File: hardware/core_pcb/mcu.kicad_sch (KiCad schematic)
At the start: 33 parts, among them J5 SWD, J6 SERVICE UART, SW1 RESET, U3 STM32H573VIT6, Y1 25MHz, Y2 32.768kHz

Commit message: Core PCB: add the 8 MB QSPI PSRAM (APS6404L) on OCTOSPI1
Gary approved the PSRAM (29 Oct) for working RAM headroom. U10 on PB2 CLK,
PB10 NCS, PB1/PB0/PC2/PA6 IO0-3 (pins agreed with the RAM thread, all
previously free), 33R series on CLK, 10k pull-up on NCS, 100n + 1u.
Project symbol APS6404L derived from KiCad's ESP-PSRAM32 (same pinout).

Co-Authored-By: Claude Opus 5.5 <noreply@anthropic.com>
Claude-Session: https://claude.ai/code/session_014onnq3eRiDkqdAB6fKiRDW
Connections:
- net PSRAM_IO2: now reaches U3.17 (PC2)
- net PSRAM_IO3: now reaches U3.31 (PA6)
- net PSRAM_IO1: now reaches U3.35 (PB0)
- net PSRAM_IO0: now reaches U3.36 (PB1)
- net PSRAM_CLK_MCU: now reaches U3.37 (PB2)
- net PSRAM_NCS: now reaches U3.47 (PB10)
- no-connect marks 43 -> 37
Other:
- moved on the sheet: C20, C23, C24, C29, C30, C33, D11, FB1, J6, JP1, R20, R21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

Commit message: Core PCB: board role jumper J7 on PE5/PE6 (CORE or I/O node)
3-pin header, GND centre, 10k pull-ups and 100n per pin. 1-2 = CORE
(PE5=0, PE6=1), 2-3 = I/O node (PE5=1, PE6=0), anything else invalid.
CORE_PCB.md section 12 and the pin map updated.

Co-Authored-By: Claude Opus 5.5 <noreply@anthropic.com>
Claude-Session: https://claude.ai/code/session_014onnq3eRiDkqdAB6fKiRDW
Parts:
- added C36, C37: 100n, Capacitor_SMD:C_0603_1608Metric, symbol Device:C
- added J7: ROLE, Connector_PinHeader_2.54mm:PinHeader_1x03_P2.54mm_Vertical, symbol Connector_Generic:Conn_01x03
- added R27, R28: 10k, Resistor_SMD:R_0603_1608Metric, symbol Device:R
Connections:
- net +3V3: now also R27.1, R28.1
- net GND: now also C36.2, C37.2, J7.2 (Pin_2)
- net ROLE_A: now reaches U3.4 (PE5)
- net ROLE_A: now also C36.1, J7.1 (Pin_1), R27.2
- net ROLE_B: now reaches U3.5 (PE6)
- net ROLE_B: now also C37.1, J7.3 (Pin_3), R28.2
- no-connect marks 37 -> 35
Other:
- note added: "FB1: VDDA / VREF+ filter C29: VCAP, CHECK value and count against the H5 datasheet Y1: HSE, CL 10 pF class. CHECK against the DK C31: CHECK for the crystal's CL Y2: CL 6 pF, ESR per AN2867 C33: AN2867, CHECK for the crystal JP1: fit a jumper for the ST bootloader"
- note added: "J6: FTDI TTL-232R-3V3 order: 1 GND, 2 CTS, 3 VCC (not connected), 4 cable TXD, 5 cable RXD, 6 RTS R23: hardware revision 0: both pulled down R25: NOT FITTED. R26: NOT FITTED. J7: shunt with pull tab; silkscreen 1-2 CORE / 2-3 I/O NODE / none = OFF; reachable only with the housing open C36: ESD, at J7"
- note added: "Notes U3: STM32H563VIT6 is pin-compatible C20: one per VDD pin, VDDUSB included C21: one per VDD pin, VDDUSB included C22: one per VDD pin, VDDUSB included C23: one per VDD pin, VDDUSB included C24: one per VDD pin, VDDUSB included C25: one per VDD pin, VDDUSB included"
- note removed: "C25: one per VDD pin, VDDUSB included FB1: VDDA / VREF+ filter C29: VCAP, CHECK value and count against the H5 datasheet Y1: HSE, CL 10 pF class. CHECK against the DK C31: CHECK for the crystal's CL Y2: CL 6 pF, ESR per AN2867"
- note removed: "C33: AN2867, CHECK for the crystal JP1: fit a jumper for the ST bootloader J6: FTDI TTL-232R-3V3 order: 1 GND, 2 CTS, 3 VCC (not connected), 4 cable TXD, 5 cable RXD, 6 RTS R23: hardware revision 0: both pulled down R25: NOT FITTED. R26: NOT FITTED."
- note removed: "Notes U3: STM32H563VIT6 is pin-compatible C20: one per VDD pin, VDDUSB included C21: one per VDD pin, VDDUSB included C22: one per VDD pin, VDDUSB included C23: one per VDD pin, VDDUSB included C24: one per VDD pin, VDDUSB included"

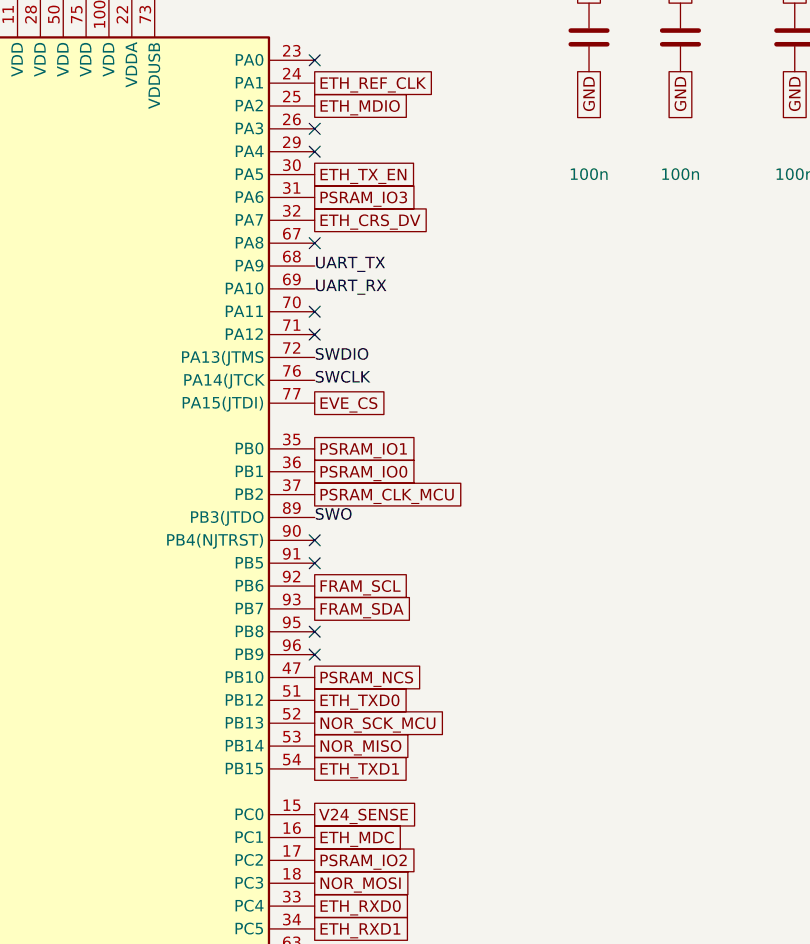
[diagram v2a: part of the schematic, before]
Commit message: Core PCB: RMII series terminations and the any-switch / 100 m design rules
33R source series resistors on TX_EN/TXD0/TXD1 (at the MCU) and
CRS_DV/RXD0/RXD1 (at the PHY), as on ST's DK. CORE_PCB.md 7 records what
the 100 m / any-switch requirement (Gary, 30 Oct) rests on: PHY crystal and
REFCLKO, MODE 111 auto-negotiation (never forced), PHY reset under firmware
control, reference line termination and differential-pair routing.

Co-Authored-By: Claude Opus 5.5 <noreply@anthropic.com>
Claude-Session: https://claude.ai/code/session_014onnq3eRiDkqdAB6fKiRDW
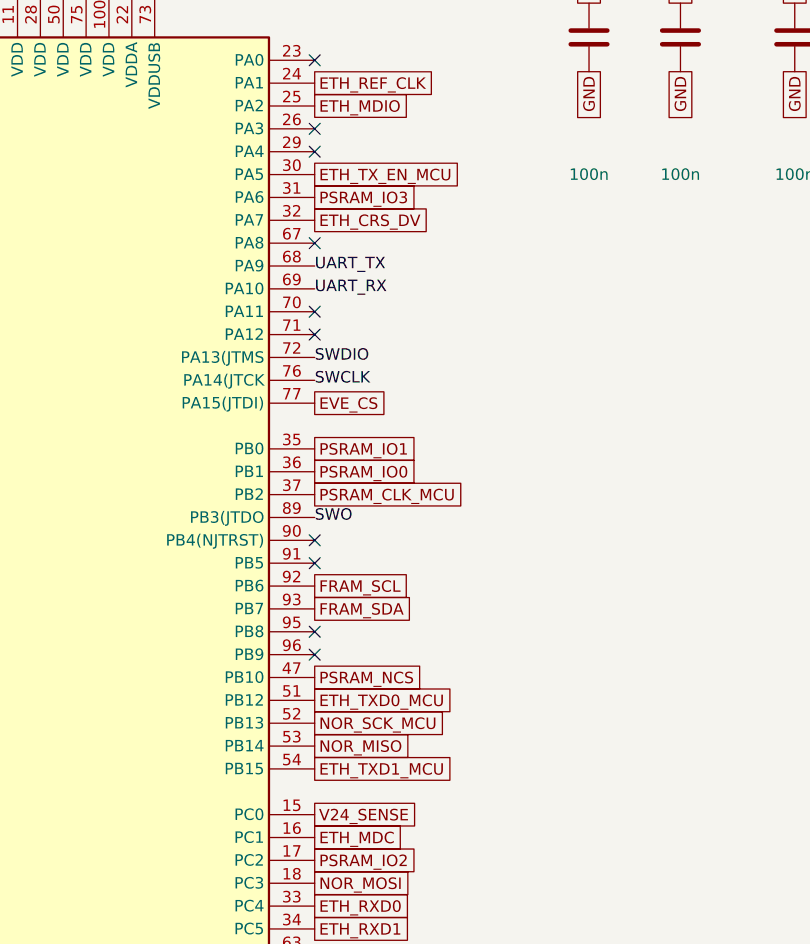
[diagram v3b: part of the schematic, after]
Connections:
- net ETH_TXD0 renamed ETH_TXD0_MCU
- net ETH_TXD1 renamed ETH_TXD1_MCU
- net ETH_TX_EN renamed ETH_TX_EN_MCU

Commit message: CORE PCB rev 0.2: I/O node section on the same board
Three new sheets: field digital I/O with the hardware output gate (ISO2H823V2.5,
ISO808A-1, ISO1I813T), field power / pump / relay coils / USB-C, and the isolated
analog (AD4112) and temperature (ADS124S08) islands. Project symbols for the six
I/O chips missing from KiCad. SPI4 nets renamed: the bus is shared with the I/O chips.
423 parts, netlist check passes. CORE_PCB.md: pin map, connectors, BOM, section 14.

Co-Authored-By: Claude Opus 5.5 <noreply@anthropic.com>
Claude-Session: https://claude.ai/code/session_014onnq3eRiDkqdAB6fKiRDW
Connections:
- net CS_A: now reaches U3.1 (PE2)
- net CS_B: now reaches U3.2 (PE3)
- net PUMP_TACH: now reaches U3.23 (PA0)
- net CS_IN: now reaches U3.3 (PE4)
- net CS_T: now reaches U3.46 (PE15)
- net GATE_FB: now reaches U3.55 (PD8)
- net B_FAULT: now reaches U3.61 (PD14)
- net B_PGOOD: now reaches U3.62 (PD15)
- net PUMP_DIR: now reaches U3.63 (PC6)
- net PUMP_EN: now reaches U3.64 (PC7)
- net USB_VBUS_SNS: now reaches U3.65 (PC8)
- net PUMP_PWM: now reaches U3.67 (PA8)
- net IN_ERR: now reaches U3.7 (PC13)
- net USB_DM: now reaches U3.70 (PA11)
- net USB_DP: now reaches U3.71 (PA12)
- net A_ERR: now reaches U3.82 (PD1)
- net REL1_N: now reaches U3.90 (PB4(NJTRST))
- net REL2_N: now reaches U3.91 (PB5)
- net GATE_EN: now reaches U3.95 (PB8)
- net WDI: now reaches U3.96 (PB9)
- net CS_AI: now reaches U3.97 (PE0)
- net W5500_MISO renamed SPI4_MISO
- net W5500_MOSI_MCU renamed SPI4_MOSI_MCU
- net W5500_SCK_MCU renamed SPI4_SCK_MCU
- no-connect marks 35 -> 14
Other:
- moved on the sheet: C20, C23, C24, C29, C30, C33, C36, C37, D11, FB1, J6, J7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
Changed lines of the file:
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@@
   (title_block
     (title "CEMS core board: MCU")
-    (date "2026-10-25")
-    (rev "0.1")
+    (date "2026-10-31")
+    (rev "0.2")
     (company "EnviroDevelo")
     (comment 1 "STM32H573VIT6, clocks, reset, boot, SWD, service UART, LEDs")

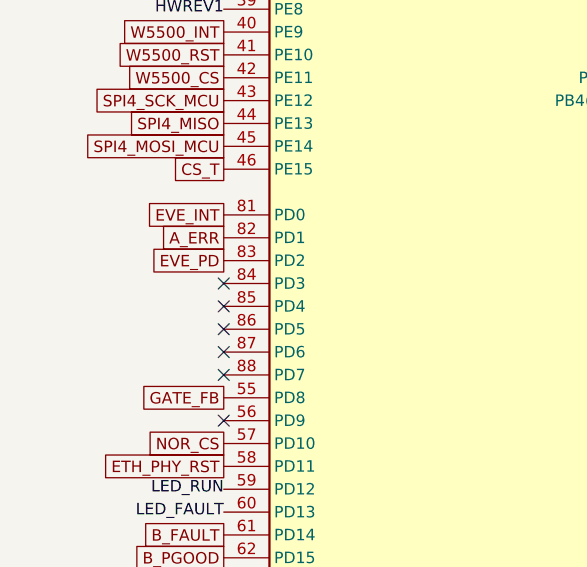
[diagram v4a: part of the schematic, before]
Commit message: CORE PCB: fit-optional 4 x 4-20 mA analog outputs (AD5755-1, all DNP)
AD5755-1 on the analog island with its own ISOW7741 (CS_AO on PD3) and an ITX2405SA for
the boost converters; keyed 8-way 3.5 mm J26 (keys 2, 6, script-checked). Pin numbers from
the datasheet Table 5. Layout block plan now 2.8 mm over in io_pwr: the board is full
single-sided, see thread for the module option.

Co-Authored-By: Claude Opus 5.5 <noreply@anthropic.com>
Claude-Session: https://claude.ai/code/session_014onnq3eRiDkqdAB6fKiRDW
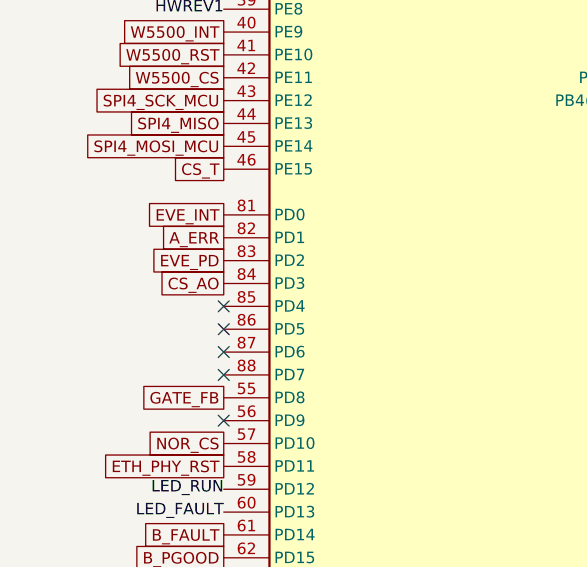
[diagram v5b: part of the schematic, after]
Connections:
- net CS_AO: now reaches U3.84 (PD3)
- no-connect marks 14 -> 13

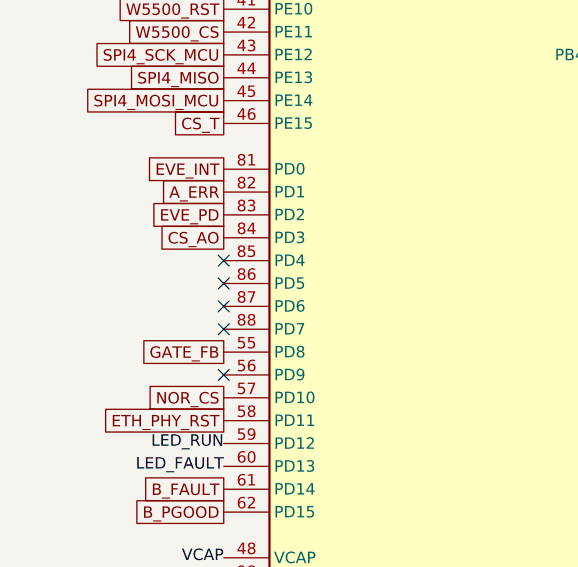
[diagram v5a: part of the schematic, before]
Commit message: CORE PCB: SPI expansion header J26 for plug-on modules; analog outputs move off the core
Gary: analog out as an add-on module. J26 10-way latched IDC: +24 V and +3.3 V behind PTCs,
SPI4 through 100R, MISO buffered by a 74LVC1G125 enabled by CS_EXP (PD3), EXP_INT on PD7.
The AD5755-1 block drafted in 04adb9f is removed from the core and will become the module.
Layout block plan fits again. CORE_PCB.md section 16.

Co-Authored-By: Claude Opus 5.5 <noreply@anthropic.com>
Claude-Session: https://claude.ai/code/session_014onnq3eRiDkqdAB6fKiRDW
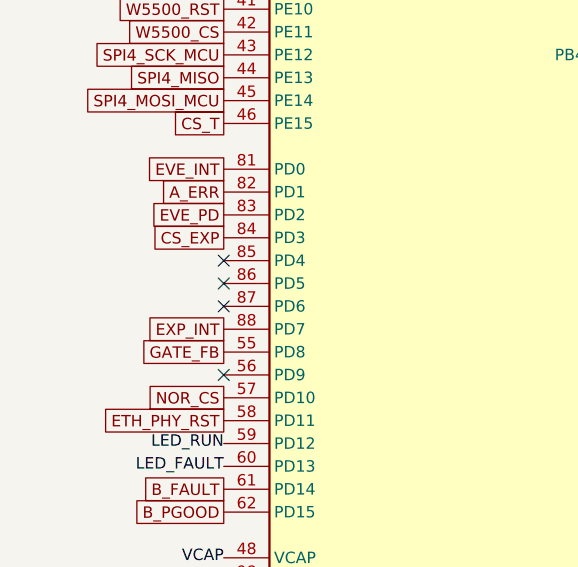
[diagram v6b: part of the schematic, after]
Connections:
- net EXP_INT: now reaches U3.88 (PD7)
- net CS_AO renamed CS_EXP
- no-connect marks 13 -> 12
